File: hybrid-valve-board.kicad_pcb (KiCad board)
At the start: 2 copper layers, 68 x 79 mm, 48 parts, among them J1 XV Supply, J10 ARM, J2 MCU Supply, J3 XV In, J4 XV In, J5 XV In, J6 Continuity, J7 XV Out, J8 XV Out, J9 XV Out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

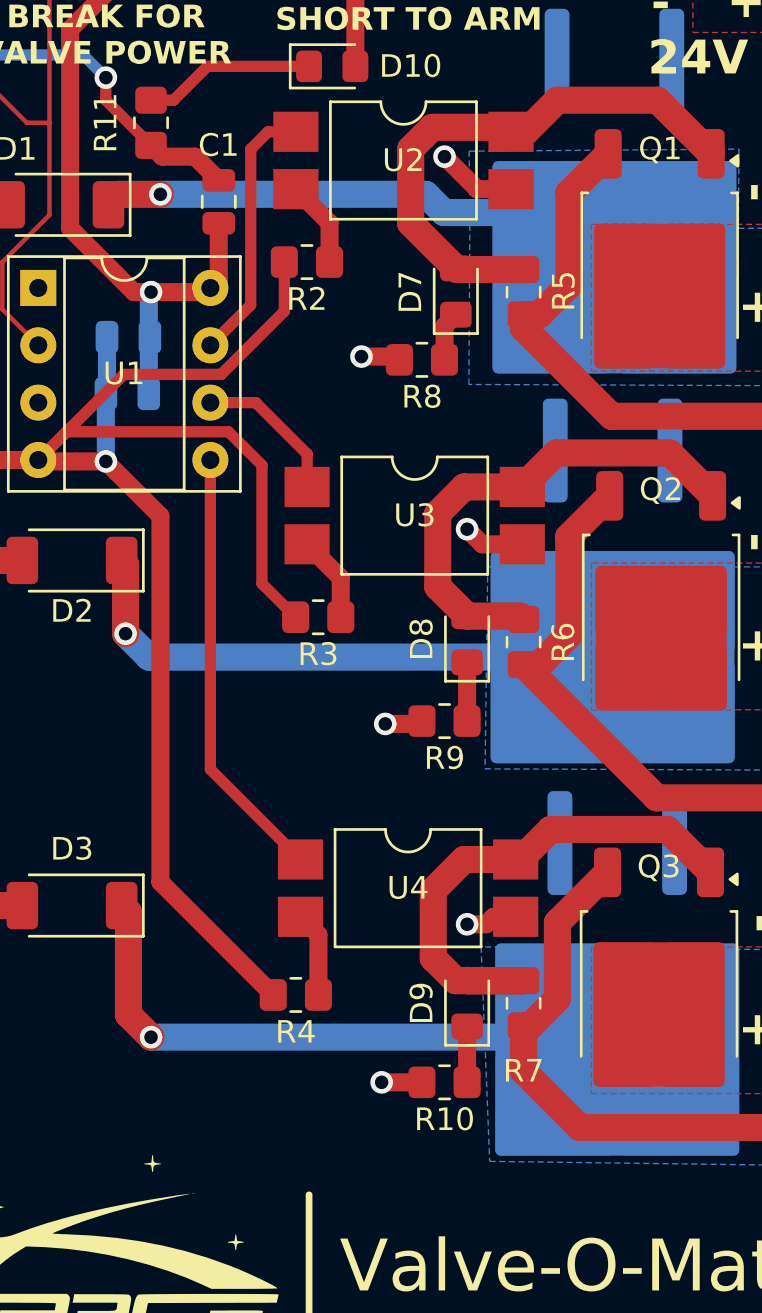
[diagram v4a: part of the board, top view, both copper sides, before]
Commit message: Move LED indicators to power line to avoid interfering with gate signal
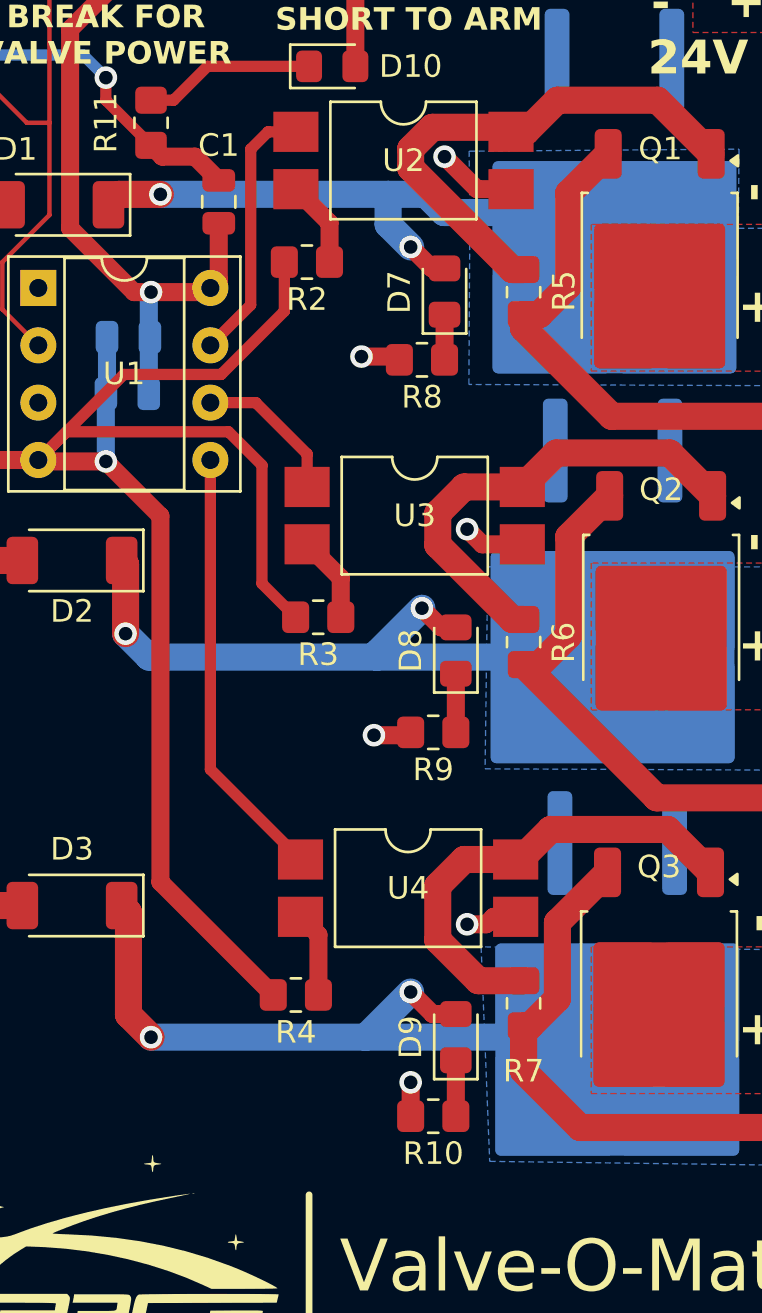
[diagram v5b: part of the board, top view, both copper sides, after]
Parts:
- moved D9 1.58 mm to (138.5, 127.0)
- moved R10 1.58 mm to (137.5, 130.5)
- moved D8 0.71 mm to (138.5, 109.9)
- moved R9 0.71 mm to (137.5, 113.5)
- moved D7 0.50 mm to (138.0, 94.0)
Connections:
- D7 pad 2: /XV4_ON_24V -> /XV4_PWR
- D8 pad 2: /XV6_ON_24V -> /XV6_PWR
- D9 pad 2: /XV7_ON_24V -> /XV7_PWR
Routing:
- net /XV7_PWR: track 29.9 -> 35.1 mm, vias 1 -> 2
- net /XV6_PWR: track 25.3 -> 30.2 mm, vias 1 -> 2
- net /XV4_PWR: track 20.2 -> 24.8 mm, vias 1 -> 2
- net /XV7_ON_24V: track 24.1 -> 20.8 mm
- net /XV4_ON_24V: track 24.5 -> 23.1 mm
- net /XV6_ON_24V: track 21.7 -> 20.6 mm

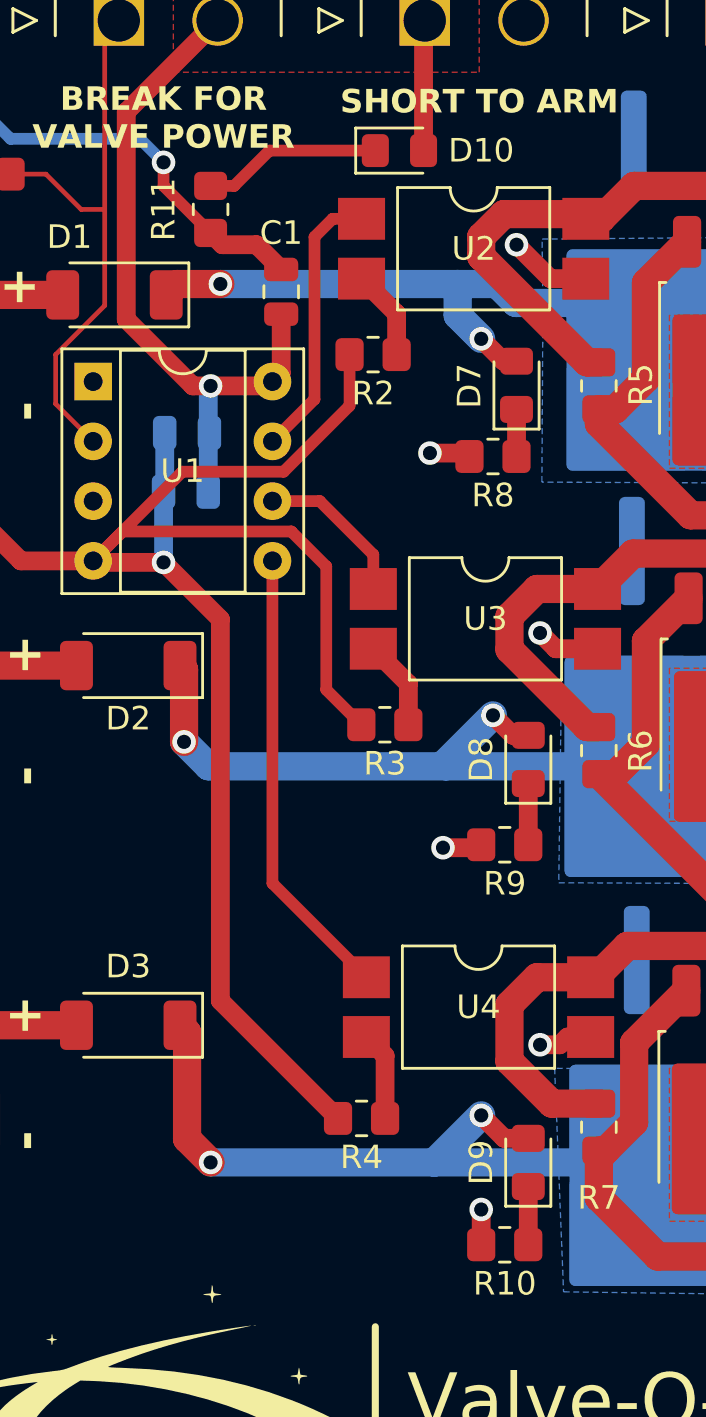
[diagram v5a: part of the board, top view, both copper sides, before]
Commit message: Use NMOS to flip opto-coupler
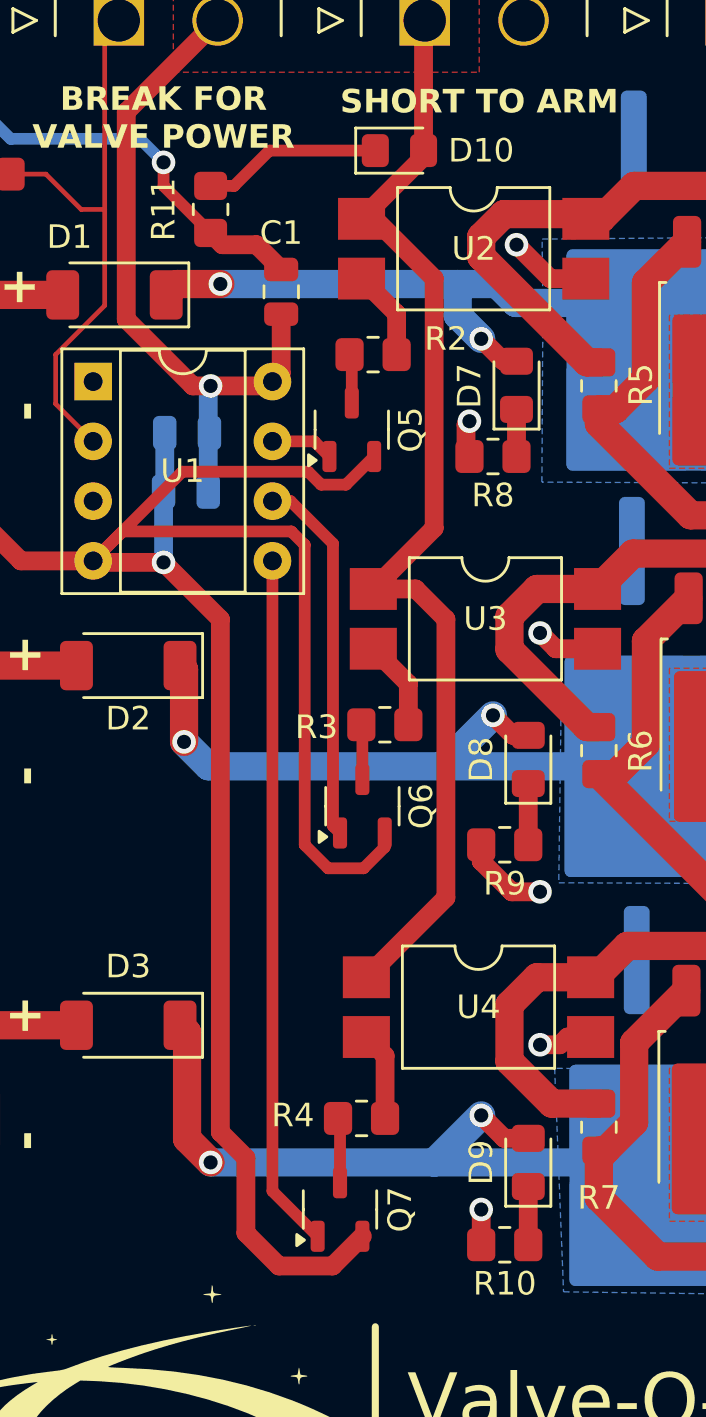
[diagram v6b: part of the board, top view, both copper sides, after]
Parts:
- added Q5: NMOS, Package_TO_SOT_SMD:SOT-23-3, F.Cu at (131.0, 95.9)
- added Q6: NMOS, Package_TO_SOT_SMD:SOT-23-3, F.Cu at (131.4, 111.9)
- added Q7: NMOS, Package_TO_SOT_SMD:SOT-23-3, F.Cu at (130.5, 129.0)
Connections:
- R2 pad 2: MCU_GND -> Net-(Q5-D)
- R3 pad 2: MCU_GND -> Net-(Q6-D)
- R4 pad 2: MCU_GND -> Net-(Q7-D)
- U2 pad 1: /XV4_ON -> VSYS
- U3 pad 1: /XV6_ON -> VSYS
- U4 pad 1: /XV7_ON -> VSYS
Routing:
- net VSYS: track 34.9 -> 77.5 mm
- net MCU_GND: track 122.4 -> 139.0 mm
- net /XV7_ON: track 19.3 -> 29.5 mm
- net /XV4_ON: track 11.7 -> 2.69 mm
- net /XV6_ON: track 6.69 -> 15.7 mm
- net Net-(Q7-D): track 0.00 -> 2.77 mm
- net Net-(Q6-D): track 0.00 -> 2.34 mm
- net Net-(Q5-D): track 0.00 -> 2.09 mm
- net GND: track 13.1 -> 15.2 mm

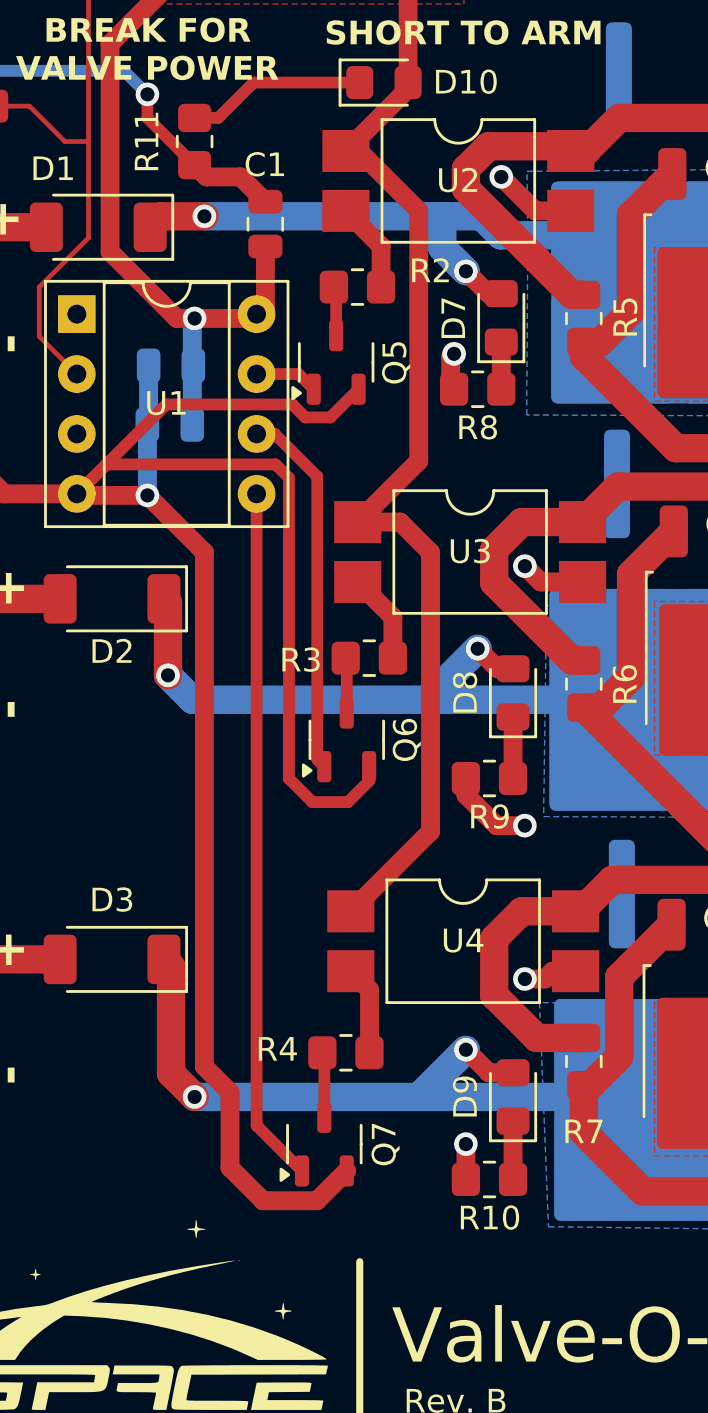
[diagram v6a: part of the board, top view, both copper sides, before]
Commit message: Add pull-down resistor on NMOS gate
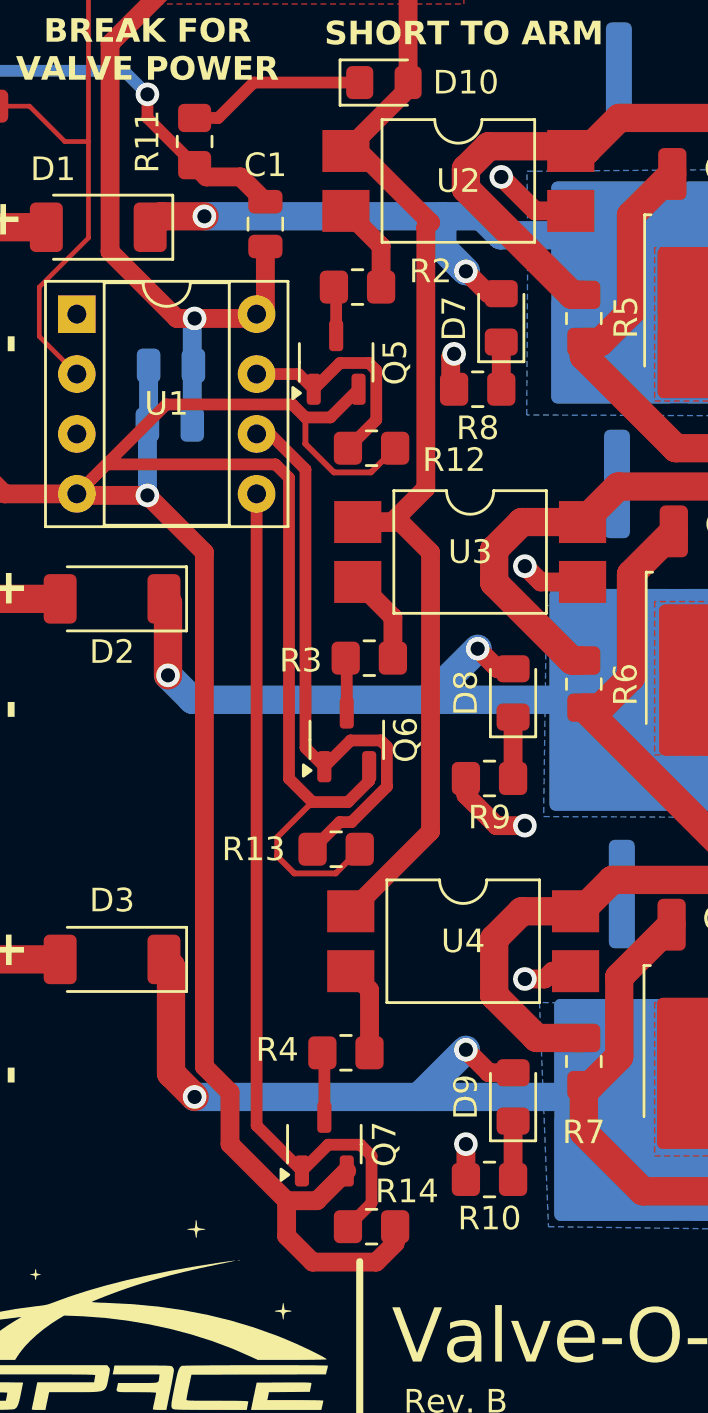
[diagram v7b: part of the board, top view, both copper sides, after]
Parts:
- added R12: 10k, Resistor_SMD:R_0805_2012Metric_Pad1.20x1.40mm_HandSolder, F.Cu at (132.5, 99.5)
- added R13: 10k, Resistor_SMD:R_0805_2012Metric_Pad1.20x1.40mm_HandSolder, F.Cu at (131.0, 116.5)
- added R14: 10k, Resistor_SMD:R_0805_2012Metric_Pad1.20x1.40mm_HandSolder, F.Cu at (132.5, 132.5)
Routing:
- net MCU_GND: track 139.0 -> 159.0 mm
- net /XV6_ON: track 15.7 -> 24.8 mm
- net /XV4_ON: track 2.69 -> 9.73 mm
- net /XV7_ON: track 29.5 -> 36.5 mm
- net VSYS: track 77.5 -> 78.8 mm
